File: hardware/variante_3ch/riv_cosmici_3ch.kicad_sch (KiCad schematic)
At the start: 178 parts, among them J101 SiPM_CH1, J104 LEMO_CH1, J201 SiPM_CH2, J204 LEMO_CH2, J3 PWR_5V, J301 SiPM_CH3, J304 LEMO_CH3, J5 LEMO_AND, Q101 BFR93A, Q102 MMBTH81, Q201 BFR93A, Q202 MMBTH81, Q301 BFR93A, Q302 MMBTH81, U1 LT3461, U10 74LVC1G11, U102 TLC555/LMC555, U103 MAX961, U108 LT1636, U109 74LVC1G17, U202 TLC555/LMC555, U203 MAX961, U208 LT1636, U209 74LVC1G17, U302 TLC555/LMC555, U303 MAX961, U308 LT1636, U309 74LVC1G17, U5 LP2985AIM5-3.6, U6 MCP1825S-3302, U7 LP2985AIM5-3.6

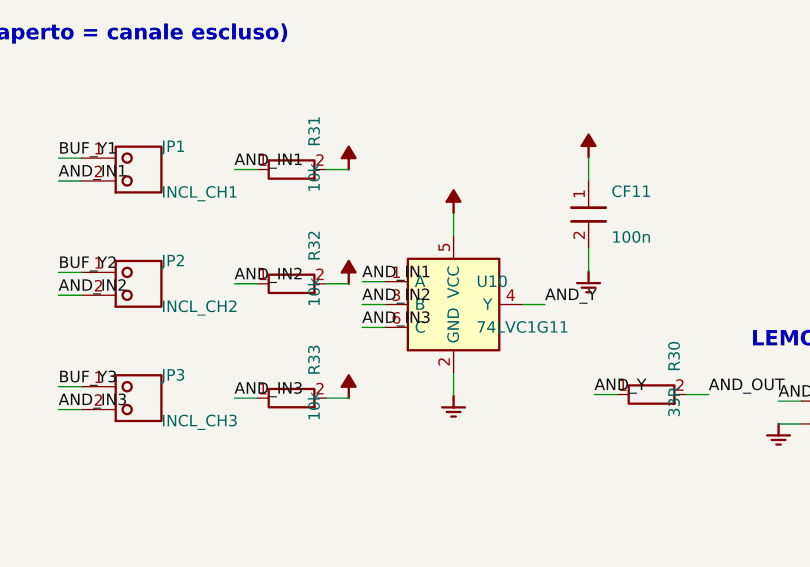
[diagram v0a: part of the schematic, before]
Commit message: Variante 3ch: PCB didattico rifatto a blocchi, test point accanto ai nodi
- piazzamento a fasce: alimentazione, 3 canali identici (segnale in alto
  da sinistra a destra, circuiti di supporto sotto), coincidenza in basso
- test point a pochi mm dal nodo misurato (SIG_IN 94 -> 9 mm di pista)
- uscite verso la coincidenza in un corridoio riservato sul bordo destro
- serigrafia didattica (silk3.py): blocchi numerati, titoli, etichette dei
  test point e dei connettori, riferimenti, schema a blocchi, legenda
  'Come funziona' sul retro; identica in KiCad (gr_poly) e nei Gerber
- ingressi dell'AND riassegnati (equivalenti) per piste senza incroci
- Keystone 5000 rosso / 5001 nero anche nella BOM

Co-Authored-By: Claude Opus 5.5 <noreply@anthropic.com>
Claude-Session: https://claude.ai/code/session_017fc9yPsNewCQrMK8R1c8Ls
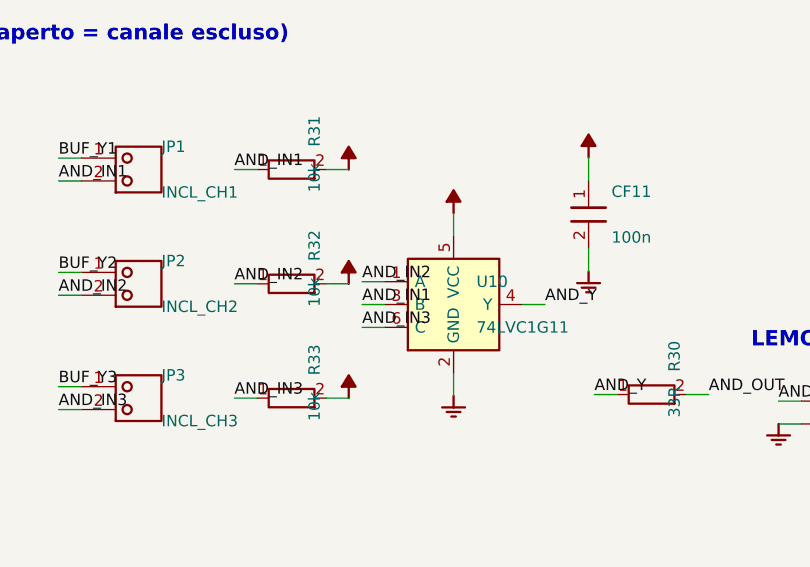
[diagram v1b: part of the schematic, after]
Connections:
- net AND_IN1: now also U10.3 (B); no longer U10.1 (A)
- net AND_IN2: now also U10.1 (A); no longer U10.3 (B)

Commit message: Variante 3ch: monitor delle tensioni dei SiPM (ADC MCP3424 in I2C)
- partitori 1M/43k + 100n su VREG38 di ogni canale e sull'alta tensione
- ADC MCP3424 (U11, 0x68), resistenze serie 100R su SDA/SCL, connettore J6
- router: le linee MON stanno a >= 1,2 mm dai nodi analogici sensibili su
  entrambi gli strati (misurato: 1,6 mm); piste dei segnali invariate
- simulazione: con il monitor bias, impulsi e soglia restano identici
- software/monitor_tensioni.py per il Raspberry Pi
- footprint SOIC14 e HDR1x03, simboli MCP3424 e CONN3; stub dei SOIC dal lato lungo

Co-Authored-By: Claude Opus 5.5 <noreply@anthropic.com>
Claude-Session: https://claude.ai/code/session_017fc9yPsNewCQrMK8R1c8Ls
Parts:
- added C150, C250, C350, C40, CF12: 100n, rivlib:C_0805, symbol riv:C
- added J6: I2C_RPI, rivlib:HDR1x03, symbol riv:CONN3
- added R150, R250, R350, R40: 1M, rivlib:R_0805, symbol riv:R
- added R151, R251, R351, R41: 43k, rivlib:R_0805, symbol riv:R
- added R42, R43: 100R, rivlib:R_0805, symbol riv:R
- added U11: MCP3424, rivlib:SOIC14, symbol riv:MCP3424
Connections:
- net +3V3: now also CF12.1, U11.6 (VDD)
- net GND: now also C150.2, C250.2, C350.2, C40.2, CF12.2, J6.1, R151.2, R251.2, R351.2, R41.2, U11.10 (A1), U11.12 (CH3-), U11.14 (CH4-), U11.2 (CH1-), U11.4 (CH2-), U11.5 (VSS), U11.9 (A0)
- net VOUT40: now also R40.1
- net VREG381: now reaches R105.2, R108.1, U108.6
- net VREG381: now also R150.1
- net VREG382: now reaches R205.2, R208.1, U208.6
- net VREG382: now also R250.1
- net VREG383: now reaches R305.2, R308.1, U308.6
- net VREG383: now also R350.1
- new net I2C_SCL: J6.3, R43.2
- new net I2C_SDA: J6.2, R42.2
- new net MON1: C150.1, R150.2, R151.1, U11.1 (CH1+)
- new net MON2: C250.1, R250.2, R251.1, U11.3 (CH2+)
- new net MON3: C350.1, R350.2, R351.1, U11.11 (CH3+)
- new net MON4: C40.1, R40.2, R41.1, U11.13 (CH4+)
- new net SCL_ADC: R43.1, U11.8 (SCL)
- new net SDA_ADC: R42.1, U11.7 (SDA)
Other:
- note added: "MONITOR TENSIONI: partitori 1M/43k su VREG38n e VOUT40 -> ADC MCP3424 (I2C, 0x68) -> Raspberry Pi"
- note added: "verso Raspberry Pi (pull-up sul Pi)"

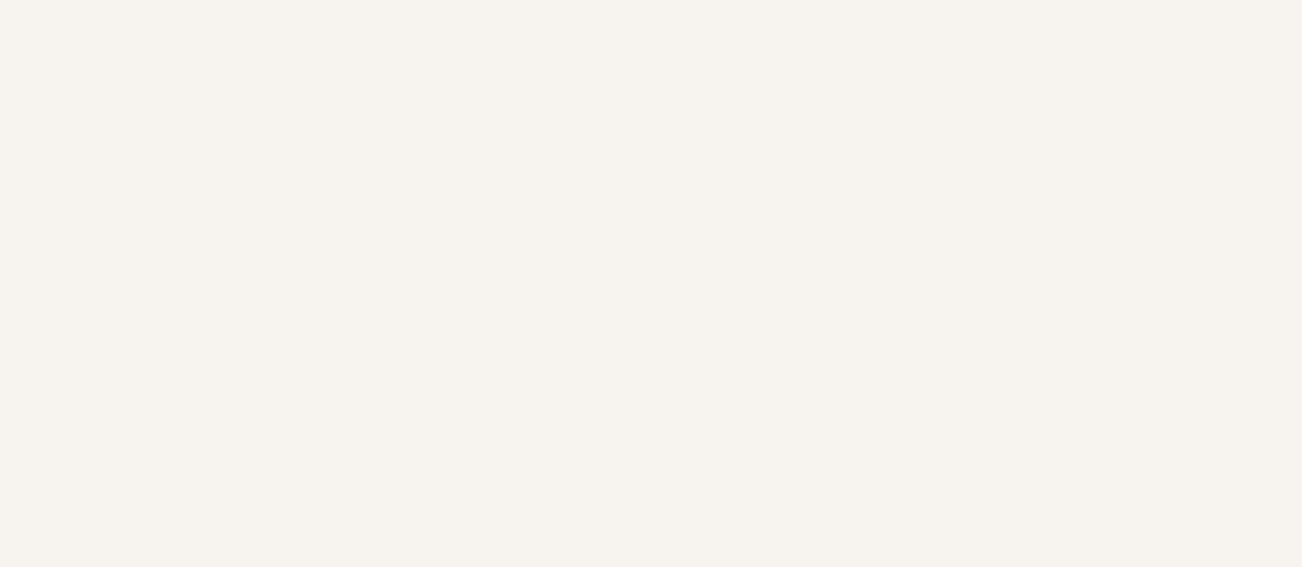
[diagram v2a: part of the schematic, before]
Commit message: Variante 3ch: disposizione piu' ordinata e fori di fissaggio M3
- scheda 103 x 215 mm: colonne distanziate (>= 2 mm tra i riquadri), spostamenti
  multipli della griglia del router
- serigrafia: riquadri della stessa riga con bordi allineati, titoli fissi,
  sottotitoli sotto il riquadro, frecce del segnale calcolate tra i blocchi,
  avviso 41 V nel blocco ALTA TENSIONE
- 8 fori M3 metallizzati a massa (angoli e confini tra i canali)
- routing rifatto: 0 errori DRC/connettivita', monitor a 1,6 mm dai nodi sensibili
- render, PDF, presentazione aggiornati

Co-Authored-By: Claude Opus 5.5 <noreply@anthropic.com>
Claude-Session: https://claude.ai/code/session_017fc9yPsNewCQrMK8R1c8Ls
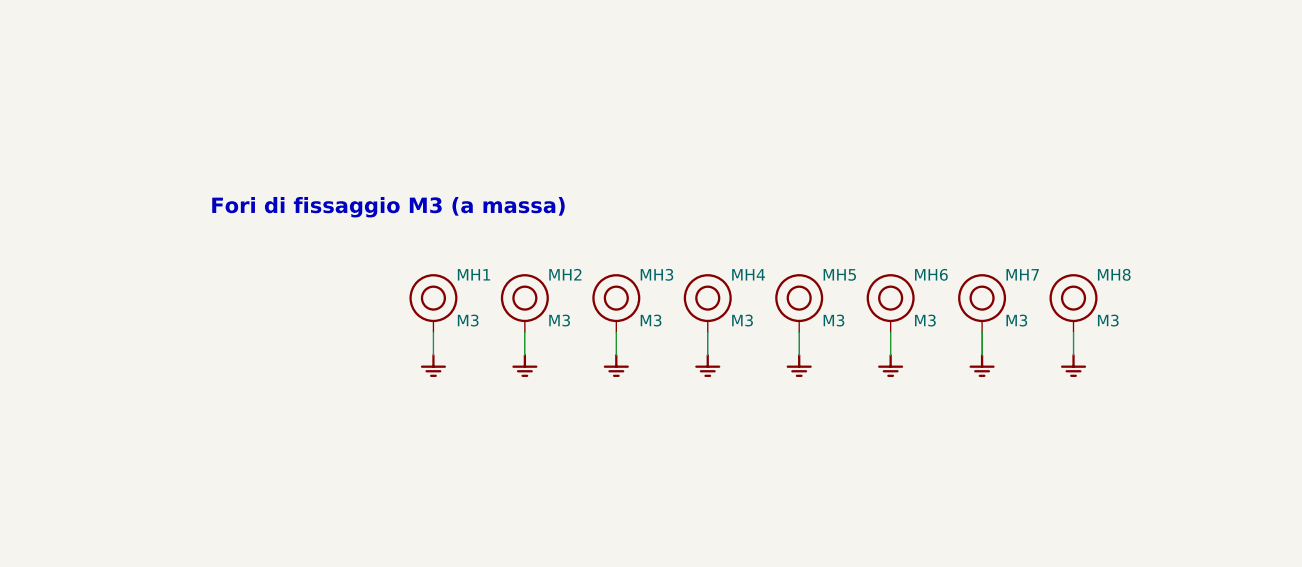
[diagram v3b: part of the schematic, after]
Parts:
- added MH1, MH2, MH3, MH4, MH5, MH6, MH7, MH8: M3, rivlib:MH_M3, symbol riv:MH
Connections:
- net GND: now also MH1.1, MH2.1, MH3.1, MH4.1, MH5.1, MH6.1, MH7.1, MH8.1
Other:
- note added: "Fori di fissaggio M3 (a massa)"

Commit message: 3 canali: connettore barra Molex KK 254 (J101/J201/J301), PCB, Gerber, JLC, PDF, librerie e render aggiornati
Footprint MOLEX_KK_2 con gli stessi fori della strip (routing invariato),
etichette 1/2 della serigrafia spostate fuori dal corpo, modello 3D del
connettore nel viewer, zip KiCad autosufficiente con librerie aggiornate.

Co-Authored-By: Claude Opus 5.5 <noreply@anthropic.com>
Claude-Session: https://claude.ai/code/session_017fc9yPsNewCQrMK8R1c8Ls
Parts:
- J101, J201, J301: footprint rivlib:HDR1x02 -> rivlib:MOLEX_KK_2

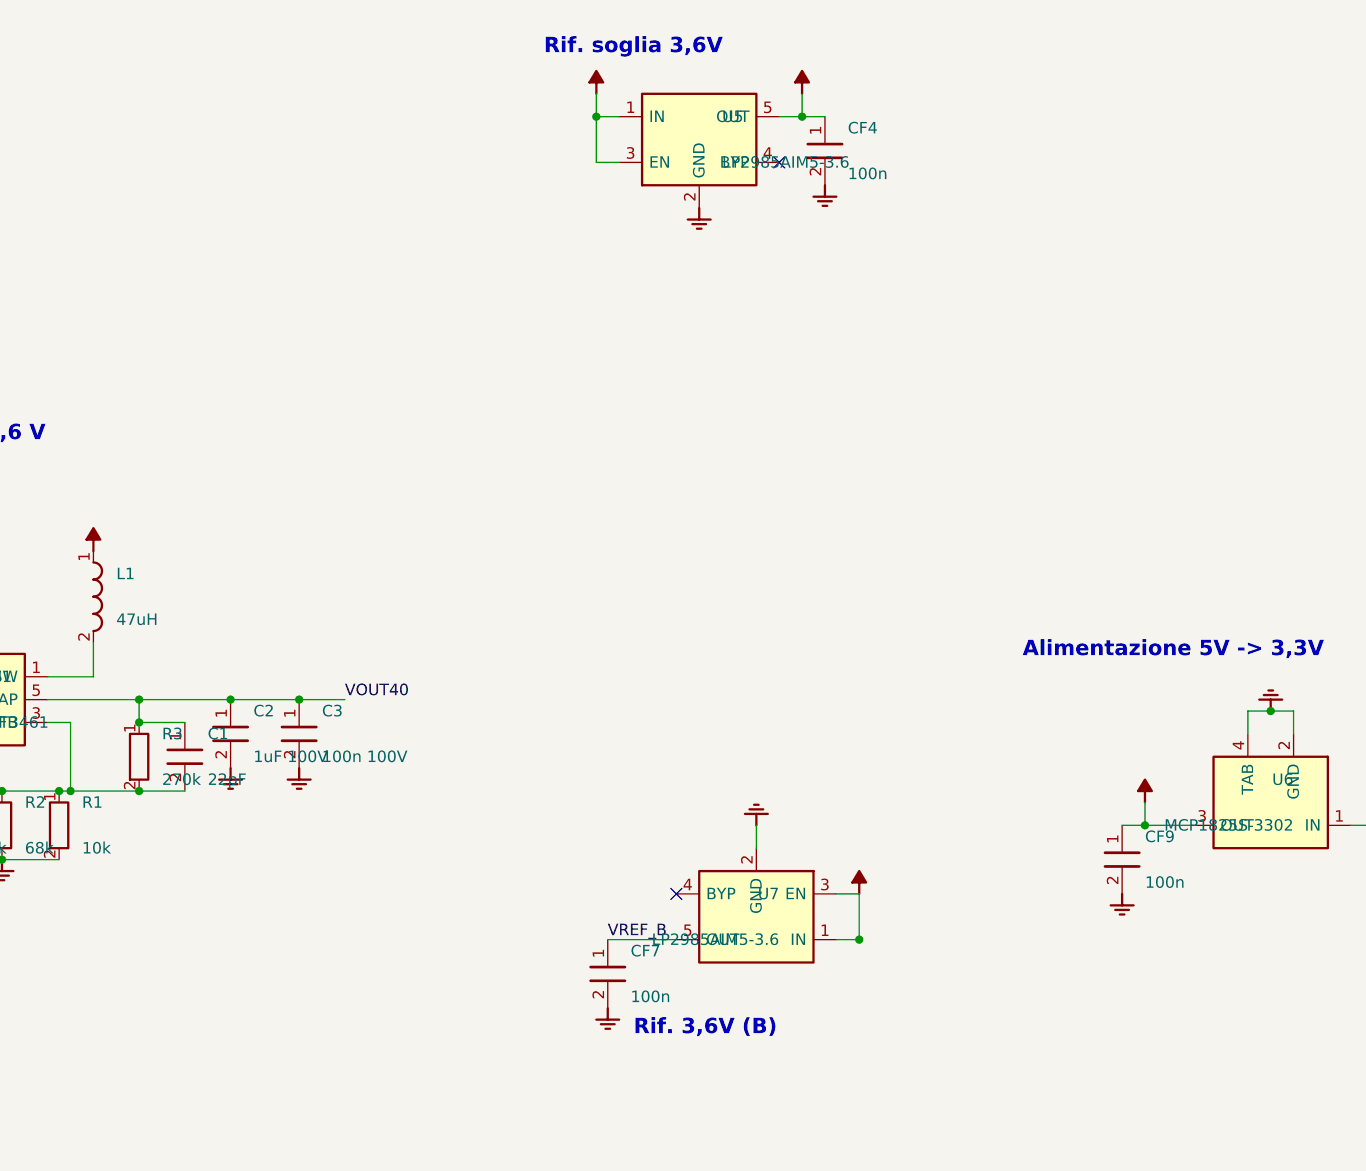
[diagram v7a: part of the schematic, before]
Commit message: R3 = 255k e 2,2 uF su CF4/CF7/CF9 (datasheet LT3461, LP2985, MCP1825), nota per la verifica INFN
- R3 270k -> 255k: VOUT40 da 41,7 a 39,4 V, sotto i 40 V max assoluti del LT3461;
  bias ancora regolabile fino a ~39,2 V (margine 1,0 V a 25 C, 0,3 V a 50 C).
- CF4, CF7, CF9 100n -> 2,2 uF X7R 0805 (Samsung CL21B225KAFNNNE): uscite dei
  regolatori, come richiesto dai datasheet.
- Schemi, PCB (valori), BOM, file JLCPCB, PDF, simulazioni e render rigenerati;
  verifica_ltspice: tutto OK; sim_3canali invariata salvo VOUT40.
- hardware/variante_3ch/NOTA_PER_TECNICO_INFN.txt: le due modifiche con calcoli,
  simulazioni e punti da verificare, piu' l'elenco delle differenze dalla scheda INFN.

Co-Authored-By: Claude Opus 5.5 <noreply@anthropic.com>
Claude-Session: https://claude.ai/code/session_017fc9yPsNewCQrMK8R1c8Ls
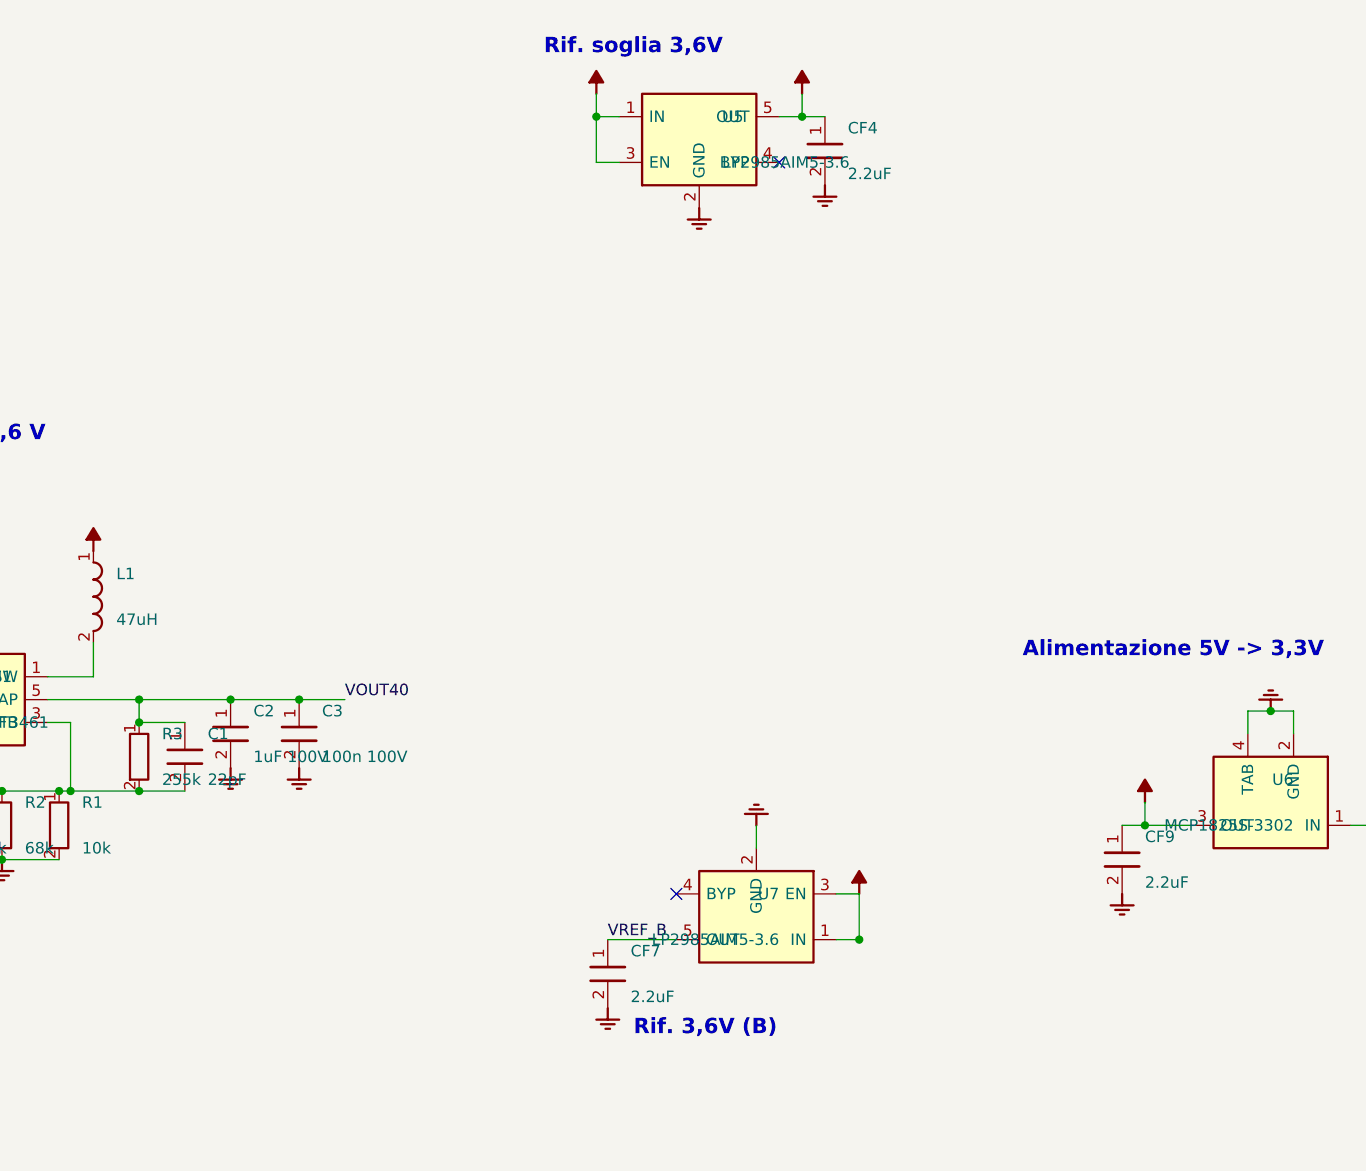
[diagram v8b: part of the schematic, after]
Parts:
- CF4, CF7, CF9: value 100n -> 2.2uF
- R3: value 270k -> 255k
